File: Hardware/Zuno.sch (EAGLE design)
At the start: 7 parts, among them Q1 2N3904, X1 5566-24

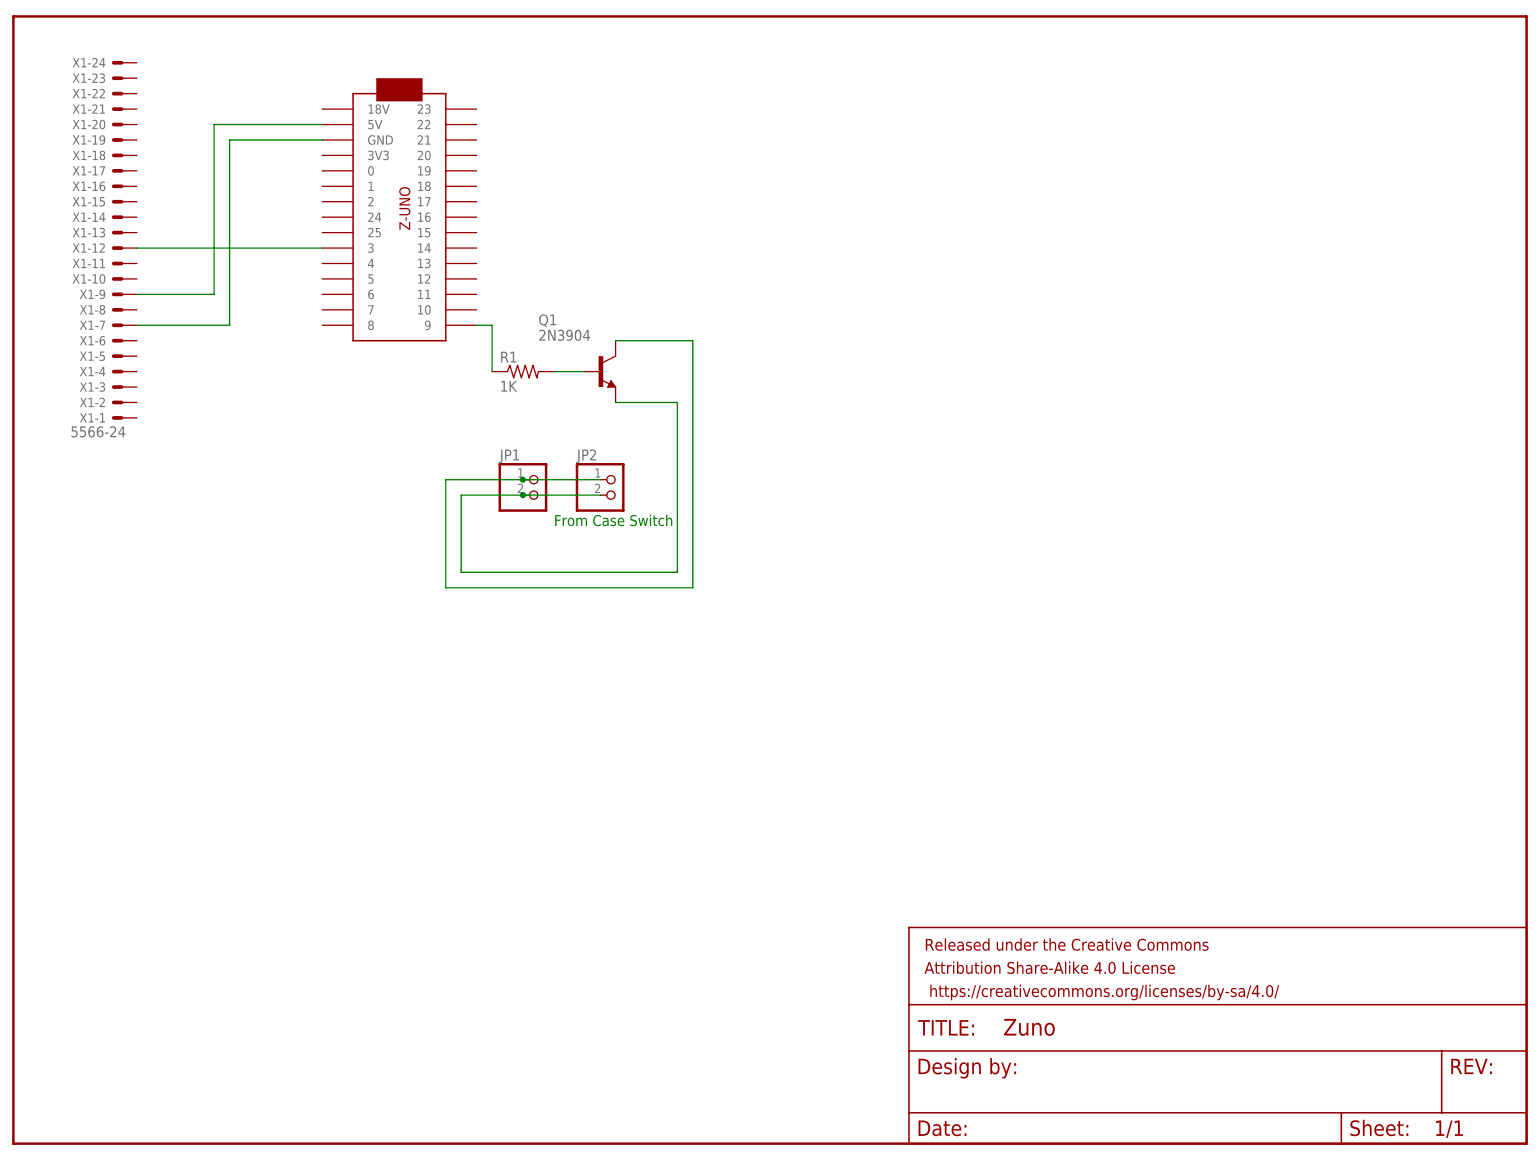
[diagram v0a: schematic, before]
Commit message: Updated board to include drill holes
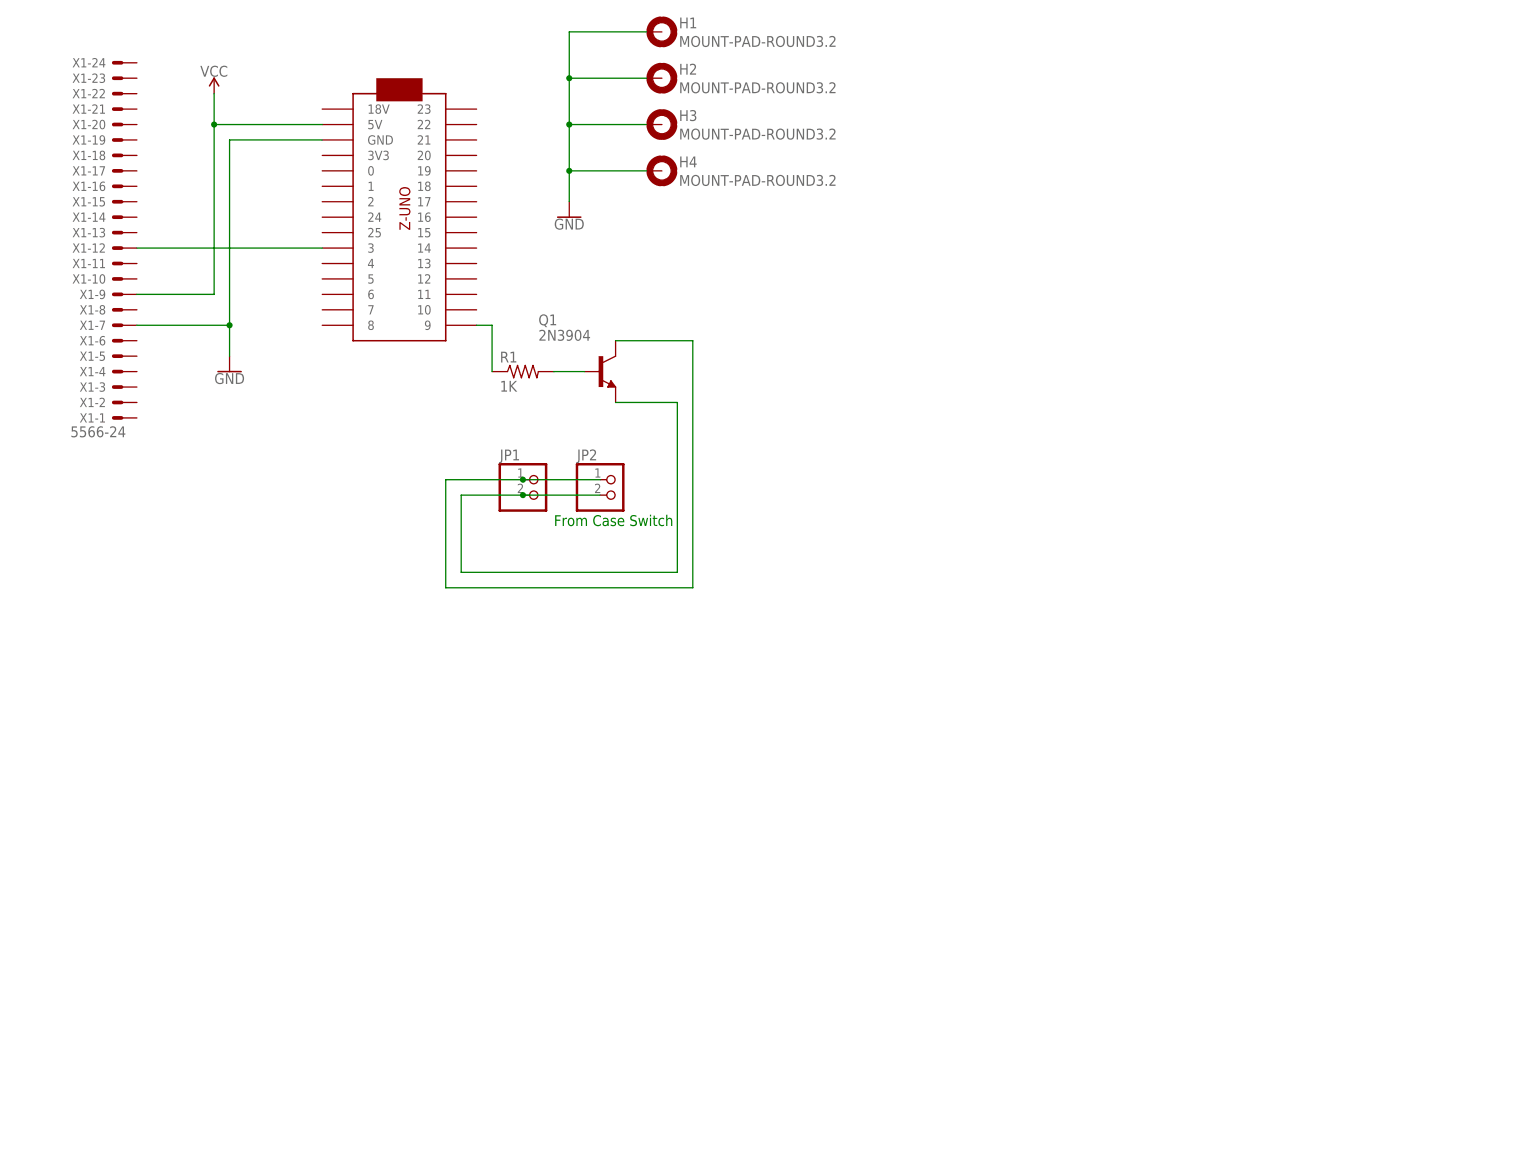
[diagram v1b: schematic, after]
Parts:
- removed FRAME1: FRAME-LETTER, SparkFun-Aesthetics:FRAME-LETTER
- added H1, H2, H3, H4: MOUNT-PAD-ROUND3.2, holes:MOUNT-PAD-ROUND3.2
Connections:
- net N$1 renamed VCC
- removed net N$2: U$1.GND, X1-7.S
- new net GND: H1.MOUNT, H2.MOUNT, H3.MOUNT, H4.MOUNT, U$1.GND, X1-7.S
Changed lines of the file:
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@@
 </classes>
 <parts>
-<part name="FRAME1" library="SparkFun-Aesthetics" library_urn="urn:adsk.eagle:library:507" deviceset="FRAME-LETTER" device=""/>
 <part name="X1" library="con-molex" library_urn="urn:adsk.eagle:library:165" deviceset="5566-24" device=""/>
 <part name="U$1" library="adafruit" deviceset="ZUNO" device=""/>
@@
 <part name="JP1" library="pinhead" library_urn="urn:adsk.eagle:library:325" deviceset="PINHD-1X2" device=""/>
 <part name="JP2" library="pinhead" library_urn="urn:adsk.eagle:library:325" deviceset="PINHD-1X2" device=""/>
+<part name="SUPPLY1" library="SparkFun-PowerSymbols" library_urn="urn:adsk.eagle:library:530" deviceset="VCC" device=""/>
+<part name="GND1" library="SparkFun-PowerSymbols" library_urn="urn:adsk.eagle:library:530" deviceset="GND" device=""/>
+<part name="H1" library="holes" library_urn="urn:adsk.eagle:library:237" deviceset="MOUNT-PAD-ROUND" device="3.2"/>
+<part name="H2" library="holes" library_urn="urn:adsk.eagle:library:237" deviceset="MOUNT-PAD-ROUND" device="3.2"/>
+<part name="H3" library="holes" library_urn="urn:adsk.eagle:library:237" deviceset="MOUNT-PAD-ROUND" device="3.2"/>
+<part name="H4" library="holes" library_urn="urn:adsk.eagle:library:237" deviceset="MOUNT-PAD-ROUND" device="3.2"/>
+<part name="GND2" library="SparkFun-PowerSymbols" library_urn="urn:adsk.eagle:library:530" deviceset="GND" device=""/>
 </parts>
 <sheets>
@@
 </plain>
 <instances>
-<instance part="FRAME1" gate="G$1" x="-7.62" y="5.08"/>
-<instance part="FRAME1" gate="V" x="139.7" y="5.08"/>
 <instance part="X1" gate="-1" x="10.16" y="124.46" rot="R180"/>
 <instance part="X1" gate="-2" x="10.16" y="127" rot="R180"/>
@@
 <instance part="JP1" gate="G$1" x="78.74" y="111.76"/>
 <instance part="JP2" gate="G$1" x="91.44" y="111.76"/>
+<instance part="SUPPLY1" gate="G$1" x="25.4" y="177.8"/>
+<instance part="GND1" gate="1" x="27.94" y="132.08"/>
+<instance part="H1" gate="G$1" x="99.06" y="187.96"/>
+<instance part="H2" gate="G$1" x="99.06" y="180.34"/>
+<instance part="H3" gate="G$1" x="99.06" y="172.72"/>
+<instance part="H4" gate="G$1" x="99.06" y="165.1"/>
+<instance part="GND2" gate="1" x="83.82" y="157.48"/>
 </instances>
 <busses>
 </busses>
 <nets>
-<net name="N$1" class="0">
-<segment>
-<pinref part="X1" gate="-9" pin="S"/>
-<wire x1="12.7" y1="144.78" x2="25.4" y2="144.78" width="0.1524" layer="91"/>
-<wire x1="25.4" y1="144.78" x2="25.4" y2="172.72" width="0.1524" layer="91"/>
-<pinref part="U$1" gate="G$1" pin="5V"/>
-<wire x1="25.4" y1="172.72" x2="43.18" y2="172.72" width="0.1524" layer="91"/>
-</segment>
-</net>
-<net name="N$2" class="0">
-<segment>
-<pinref part="X1" gate="-7" pin="S"/>
-<wire x1="12.7" y1="139.7" x2="27.94" y2="139.7" width="0.1524" layer="91"/>
-<wire x1="27.94" y1="139.7" x2="27.94" y2="170.18" width="0.1524" layer="91"/>
-<pinref part="U$1" gate="G$1" pin="GND"/>
-<wire x1="27.94" y1="170.18" x2="43.18" y2="170.18" width="0.1524" layer="91"/>
-</segment>
-</net>
 <net name="N$3" class="0">
 <segment>
@@
 </segment>
 </net>
+<net name="VCC" class="0">
+<segment>
+<pinref part="X1" gate="-9" pin="S"/>
+<wire x1="12.7" y1="144.78" x2="25.4" y2="144.78" width="0.1524" layer="91"/>
+<wire x1="25.4" y1="144.78" x2="25.4" y2="172.72" width="0.1524" layer="91"/>
+<pinref part="U$1" gate="G$1" pin="5V"/>
+<wire x1="25.4" y1="172.72" x2="43.18" y2="172.72" width="0.1524" layer="91"/>
+<pinref part="SUPPLY1" gate="G$1" pin="VCC"/>
+<wire x1="25.4" y1="172.72" x2="25.4" y2="177.8" width="0.1524" layer="91"/>
+<junction x="25.4" y="172.72"/>
+</segment>
+</net>
+<net name="GND" class="0">
+<segment>
+<pinref part="X1" gate="-7" pin="S"/>
+<wire x1="12.7" y1="139.7" x2="27.94" y2="139.7" width="0.1524" layer="91"/>
+<wire x1="27.94" y1="139.7" x2="27.94" y2="170.18" width="0.1524" layer="91"/>
+<pinref part="U$1" gate="G$1" pin="GND"/>
+<wire x1="27.94" y1="170.18" x2="43.18" y2="170.18" width="0.1524" layer="91"/>
+<pinref part="GND1" gate="1" pin="GND"/>
+<wire x1="27.94" y1="139.7" x2="27.94" y2="134.62" width="0.1524" layer="91"/>
+<junction x="27.94" y="139.7"/>
+</segment>
+<segment>
+<pinref part="H1" gate="G$1" pin="MOUNT"/>
+<wire x1="96.52" y1="187.96" x2="83.82" y2="187.96" width="0.1524" layer="91"/>
+<pinref part="GND2" gate="1" pin="GND"/>
+<wire x1="83.82" y1="187.96" x2="83.82" y2="180.34" width="0.1524" layer="91"/>
+<wire x1="83.82" y1="180.34" x2="83.82" y2="172.72" width="0.1524" layer="91"/>
+<wire x1="83.82" y1="172.72" x2="83.82" y2="165.1" width="0.1524" layer="91"/>
+<pinref part="H3" gate="G$1" pin="MOUNT"/>
+<wire x1="83.82" y1="165.1" x2="83.82" y2="160.02" width="0.1524" layer="91"/>
+<wire x1="96.52" y1="172.72" x2="83.82" y2="172.72" width="0.1524" layer="91"/>
+<junction x="83.82" y="172.72"/>
+<pinref part="H2" gate="G$1" pin="MOUNT"/>
+<wire x1="96.52" y1="180.34" x2="83.82" y2="180.34" width="0.1524" layer="91"/>
+<junction x="83.82" y="180.34"/>
+<pinref part="H4" gate="G$1" pin="MOUNT"/>
+<wire x1="96.52" y1="165.1" x2="83.82" y2="165.1" width="0.1524" layer="91"/>
+<junction x="83.82" y="165.1"/>
+</segment>
+</net>
 </nets>
 </sheet>
 </sheets>
+<errors>
+</errors>
 </schematic>
 </drawing>
